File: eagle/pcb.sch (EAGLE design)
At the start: 75 parts, among them X1 16 MHz, X2 12 MHz

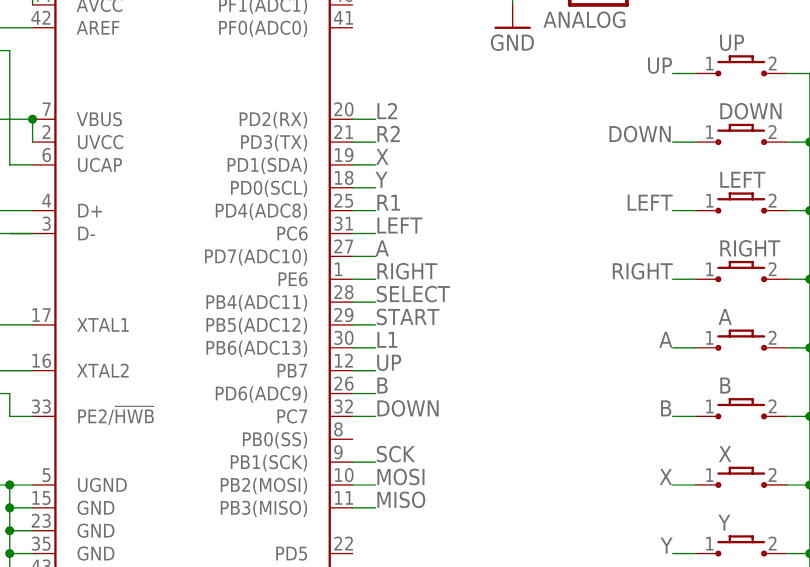
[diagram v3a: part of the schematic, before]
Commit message: v0.3, moved the left shoulder away from rpi zero
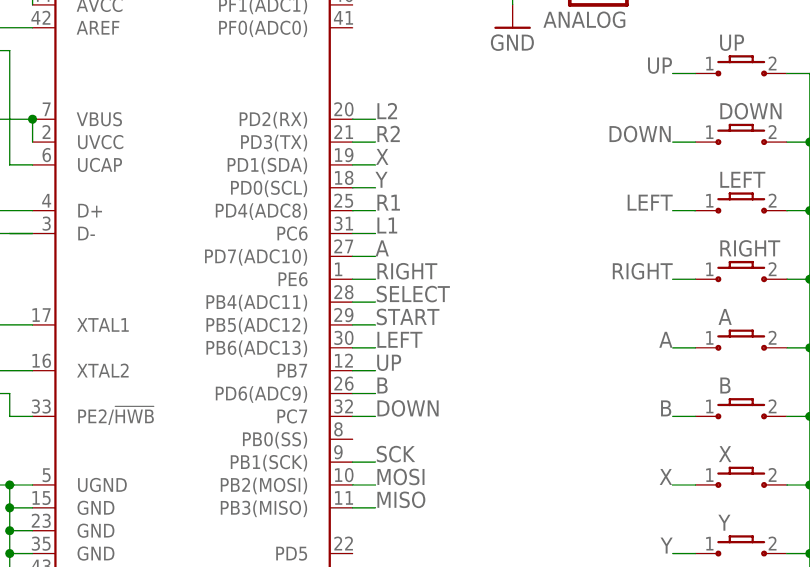
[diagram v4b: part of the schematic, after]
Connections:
- net L1: now also U$1.PC6; no longer U$1.PB6(ADC13)
- net LEFT: now also U$1.PB6(ADC13); no longer U$1.PC6
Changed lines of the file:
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@@
 </segment>
 <segment>
-<pinref part="U$1" gate="G$1" pin="PC6"/>
-<wire x1="203.2" y1="114.3" x2="205.74" y2="114.3" width="0.1524" layer="91"/>
-<label x="205.74" y="114.3" size="1.778" layer="95"/>
+<pinref part="U$1" gate="G$1" pin="PB6(ADC13)"/>
+<wire x1="203.2" y1="101.6" x2="205.74" y2="101.6" width="0.1524" layer="91"/>
+<label x="205.74" y="101.6" size="1.778" layer="95"/>
 </segment>
 </net>
@@
 </segment>
 <segment>
-<pinref part="U$1" gate="G$1" pin="PB6(ADC13)"/>
-<wire x1="203.2" y1="101.6" x2="205.74" y2="101.6" width="0.1524" layer="91"/>
-<label x="205.74" y="101.6" size="1.778" layer="95"/>
+<pinref part="U$1" gate="G$1" pin="PC6"/>
+<wire x1="203.2" y1="114.3" x2="205.74" y2="114.3" width="0.1524" layer="91"/>
+<label x="205.74" y="114.3" size="1.778" layer="95"/>
 </segment>
 </net>
